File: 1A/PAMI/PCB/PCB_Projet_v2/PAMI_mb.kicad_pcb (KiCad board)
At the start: 4 copper layers, 65 x 56 mm, 106 parts, among them J101 Conn_02x20_Odd_Even, J102 Conn_01x03, J103 Conn_ST_STDC14, J104 Battery, J105 Charge, J106 Stop, J107 Conn_01x04, J108 173010542, J109 Conn_01x04, J110 Conn_01x04, J111 Conn_01x04, J112 Conn_01x04, SW101 SW_Push_SPDT, SW102 RotaryEncoder_Switch, SW103 SW_Push, SW401 SW_Push, SW501 SW_Push, SW601 SW_Push, U101 STM32G431KBTx, U102 LT1076CR-PBF, U103 AZ1117CH2-3.3TRG1, U201 TMC2225-SA-T, U301 TMC2225-SA-T

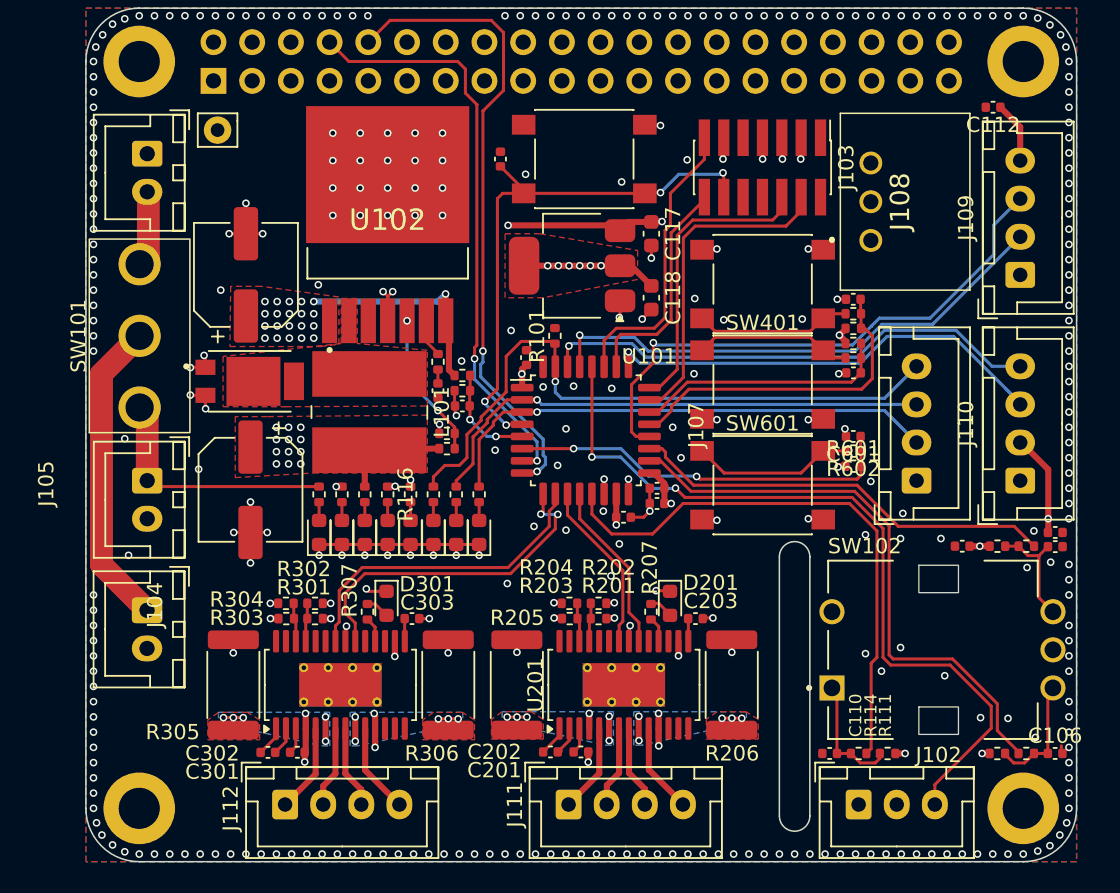
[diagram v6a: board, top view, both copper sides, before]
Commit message: update PCB Silkcreen
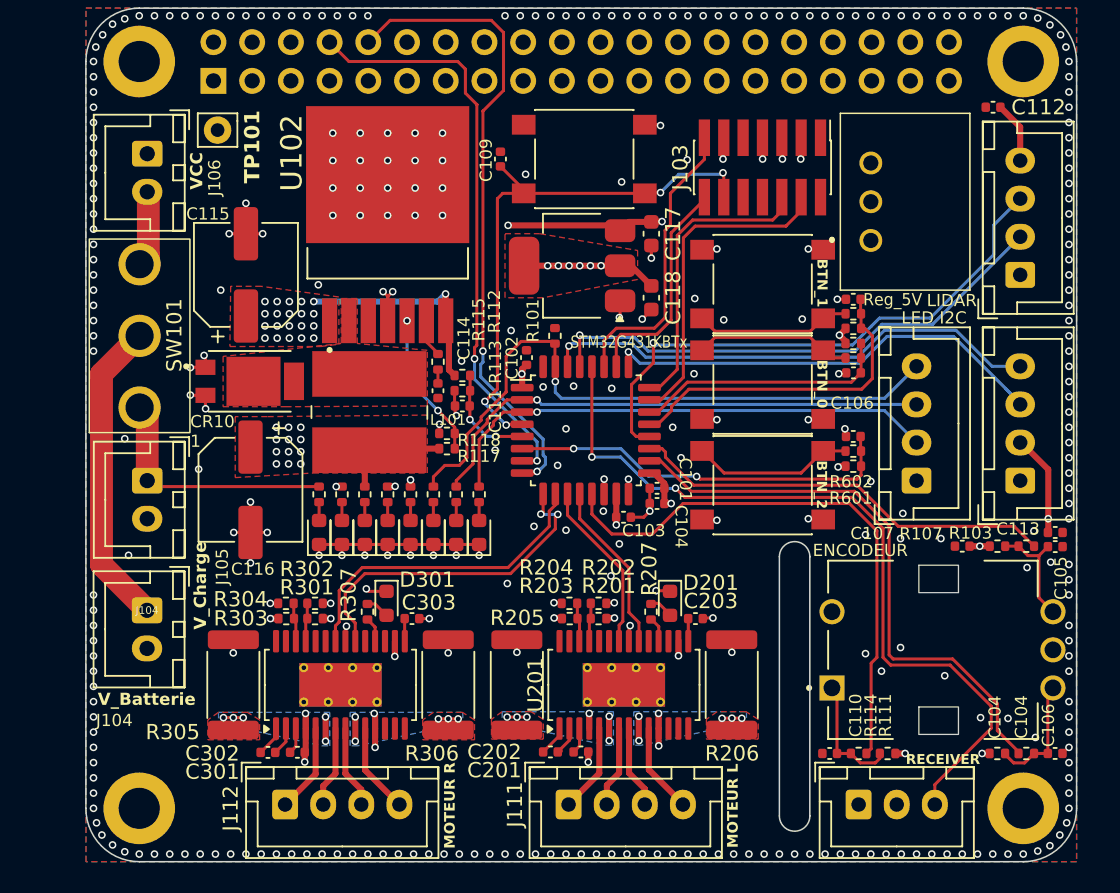
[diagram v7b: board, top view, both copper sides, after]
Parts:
- renumbered SW102 to ENCODEUR, J109 to LIDAR, J102 to RECEIVER, U101 to STM32G431KBTx
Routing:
- net GND: track 69.1 -> 68.6 mm
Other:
- board text added: "BTN_0"
- board text added: "BTN_1"
- board text added: "BTN_2"
- board text added: "C101"
- board text added: "C102"
- board text added: "C103"
- board text added: "C104"
- board text added: "C105"
- board text added: "C106"
- board text added: "C107"
- board text added: "C109"
- board text added: "C111"
- board text added: "C113"
- board text added: "C114"
- board text added: "C115"
- board text added: "C116"
- board text added: "CR10 1"
- board text added: "D101"
- board text added: "D102"
- board text added: "D103"
- board text added: "D104"
- board text added: "D105"
- board text added: "D106"
- board text added: "D107"
- board text added: "D108"
- board text added: "I2C"
- board text added: "J104"
- board text added: "J106"
- board text added: "LED"
- board text added: "MOTEUR L"
- board text added: "MOTEUR R"
- board text added: "R102"
- board text added: "R103"
- board text added: "R104"
- board text added: "R106"
- board text added: "R107"
- board text added: "R108"
- board text added: "R110"
- board text added: "R112"
- board text added: "R113"
- board text added: "R115"
- board text added: "R117"
- board text added: "R118"
- board text added: "R119"
- board text added: "R120"
- board text added: "R601"
- board text added: "R602"
- board text added: "Reg_5V"
- board text added: "SW601"
- board text added: "TP101"
- board text added: "VCC"
- board text added: "V_Batterie"
- board text added: "V_Charge"

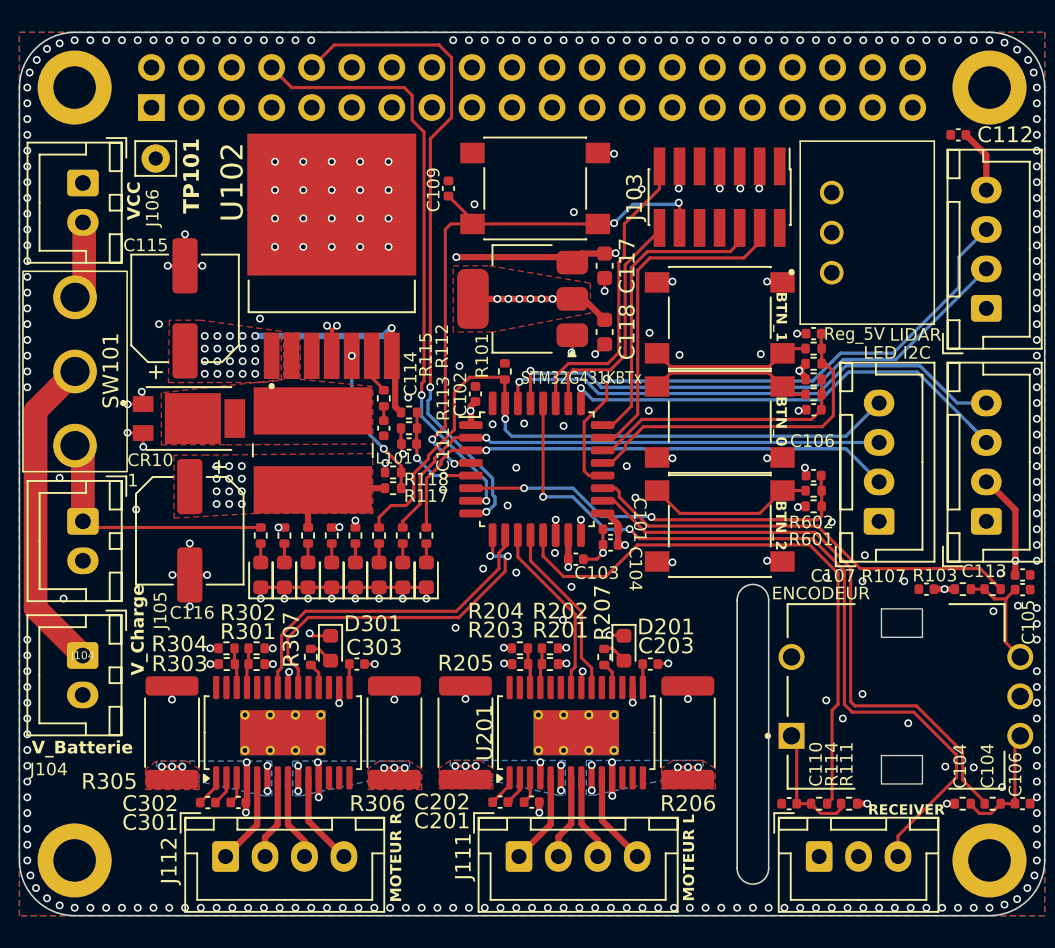
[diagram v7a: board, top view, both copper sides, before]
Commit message: update PCB Silkscreen
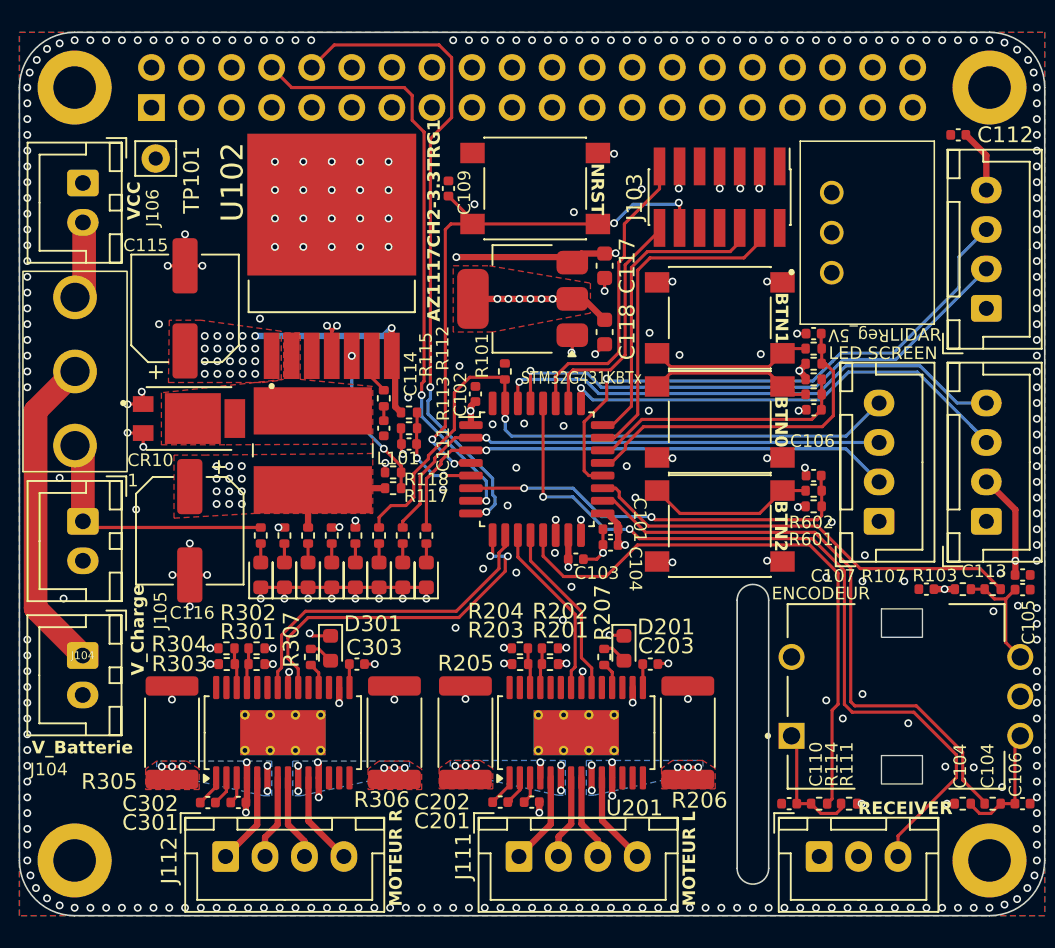
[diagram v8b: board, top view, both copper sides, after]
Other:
- board text added: "AZ1117CH2-3.3TRG1"
- board text added: "BTN0"
- board text added: "BTN1"
- board text added: "BTN2"
- board text added: "NRST"
- board text added: "SCREEN"
- board text added: "SW103"
- board text removed: "BTN_0"
- board text removed: "BTN_1"
- board text removed: "BTN_2"
- board text removed: "I2C"
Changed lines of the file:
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@@
 		(tags "resistor")
 		(property "Reference" "R116"
-			(at 0.040151 0.788143 270)
+			(at 0.040151 0.788143 -90)
 			(layer "B.SilkS")
 			(effects
@@
 		(tags "resistor")
 		(property "Reference" "R101"
-			(at 1 -1.442477 270)
+			(at 1 -1.442477 -90)
 			(layer "F.SilkS")
 			(effects
@@
 				(font
 					(size 1.4 1.4)
-					(thickness 0.15)
+					(thickness 0.2)
 				)
 			)
@@
 		(tags "resistor")
 		(property "Reference" "R206"
-			(at -4.5 0.025 0)
+			(at -4.28968 0.735407 0)
 			(layer "F.SilkS")
 			(effects
@@
 		(tags "connector JST XH vertical")
 		(property "Reference" "RECEIVER"
-			(at 5.53124 -2.963175 0)
+			(at 5.462581 -3.05864 0)
 			(layer "F.SilkS" knockout)
 			(effects
 				(font
-					(size 0.65 0.65)
+					(size 0.8 0.8)
 					(thickness 0.125)
 					(bold yes)
@@
 			(at 0.049282 2.27866 90)
 			(unlocked yes)
-			(layer "F.SilkS")
+			(layer "B.SilkS")
 			(effects
 				(font
@@
 					(thickness 0.1)
 				)
+				(justify mirror)
 			)
 		)
@@
 		(tags "resistor")
 		(property "Reference" "R306"
-			(at -4.5 -1.075 0)
+			(at -4.246477 -0.800908 0)
 			(layer "F.SilkS")
 			(effects
@@
 		(tags "HTSSOP SO")
 		(property "Reference" "U201"
-			(at 0 -5.8 -90)
+			(at -4.774704 3.690625 0)
 			(layer "F.SilkS")
 			(effects
@@
 		(tags "Choke Power Inductor WE-PD2 TypL Wuerth")
 		(property "Reference" "L101"
-			(at 0.514116 -5.160024 180)
+			(at 0.514116 -5.4 180)
 			(layer "F.SilkS")
 			(effects
 				(font
-					(size 0.7 0.7)
+					(size 0.8 0.8)
 					(thickness 0.15)
 				)
@@
 		(tags "resistor")
 		(property "Reference" "R602"
-			(at -1.15 -0.051702 270)
+			(at -1.15 -0.051702 -90)
 			(layer "F.SilkS")
 			(hide yes)
@@
 		)
 	)
+	(gr_text "SW103"
+		(at 161.819337 56.780738 0)
+		(layer "B.SilkS")
+		(effects
+			(font
+				(size 1 1)
+				(thickness 0.15)
+			)
+			(justify left bottom mirror)
+		)
+	)
 	(gr_text "D108"
 		(at 148.262923 82.605614 90)
@@
 		)
 	)
+	(gr_text "NRST"
+		(at 162.672215 54.788608 270)
+		(layer "F.SilkS")
+		(effects
+			(font
+				(size 0.8 0.8)
+				(thickness 0.2)
+				(bold yes)
+			)
+			(justify left bottom)
+		)
+	)
 	(gr_text "C104"
 		(at 186.610343 94.452818 90)
@@
 	)
 	(gr_text "R112"
-		(at 153.768899 67.822679 90)
+		(at 153.797157 67.954768 90)
 		(layer "F.SilkS")
 		(effects
@@
 		)
 	)
-	(gr_text "BTN_0"
-		(at 174.403692 69.560034 -90)
+	(gr_text "BTN0"
+		(at 174.313433 69.550519 270)
 		(layer "F.SilkS" knockout)
 		(effects
 			(font
-				(size 0.67 0.67)
+				(size 0.8 0.8)
 				(thickness 0.1675)
 				(bold yes)
@@
 	)
 	(gr_text "C109"
-		(at 153.224734 57.908091 90)
+		(at 155.1748 58.090408 90)
 		(layer "F.SilkS")
 		(effects
@@
 		)
 	)
-	(gr_text "BTN_2"
-		(at 174.380489 76.167315 -90)
+	(gr_text "BTN2"
+		(at 174.301377 76.171212 270)
 		(layer "F.SilkS" knockout)
 		(effects
 			(font
-				(size 0.67 0.67)
+				(size 0.8 0.8)
 				(thickness 0.1675)
 				(bold yes)
@@
 			(font
 				(size 1 1)
-				(thickness 0.2)
-				(bold yes)
+				(thickness 0.1)
 			)
 			(justify left bottom)
@@
 	)
 	(gr_text "LED"
-		(at 180 67.286825 0)
+		(at 177.795686 67.304999 0)
 		(layer "F.SilkS" knockout)
 		(effects
@@
 	)
 	(gr_text "MOTEUR R"
-		(at 150.78488 101.657029 90)
+		(at 150.831816 101.909537 90)
 		(layer "F.SilkS" knockout)
 		(effects
 			(font
-				(size 0.7 0.7)
+				(size 0.8 0.76)
 				(thickness 0.125)
 				(bold yes)
@@
 		)
 	)
+	(gr_text "AZ1117CH2-3.3TRG1"
+		(at 153.248634 64.845979 90)
+		(layer "F.SilkS")
+		(effects
+			(font
+				(size 0.8 0.8)
+				(thickness 0.2)
+				(bold yes)
+			)
+			(justify left bottom)
+		)
+	)
 	(gr_text "C106"
 		(at 175.348619 72.880489 0)
@@
 	)
 	(gr_text "MOTEUR L"
-		(at 169.352696 101.605055 90)
+		(at 169.430681 101.898404 90)
 		(layer "F.SilkS" knockout)
 		(effects
 			(font
-				(size 0.7 0.7)
+				(size 0.8 0.76)
 				(thickness 0.125)
 				(bold yes)
@@
 		)
 	)
-	(gr_text "I2C"
-		(at 182.5 67.286825 0)
+	(gr_text "SCREEN"
+		(at 180.27125 67.311931 0)
 		(layer "F.SilkS" knockout)
 		(effects
@@
 		)
 	)
-	(gr_text "BTN_1"
-		(at 174.413838 62.938578 -90)
+	(gr_text "BTN1"
+		(at 174.349311 62.981348 270)
 		(layer "F.SilkS" knockout)
 		(effects
 			(font
-				(size 0.67 0.67)
+				(size 0.8 0.8)
 				(thickness 0.1675)
 				(bold yes)
@@
 	)
 	(gr_text "Reg_5V"
-		(at 177.496389 66.091718 0)
+		(at 181.647312 65.241175 180)
 		(layer "F.SilkS")
 		(effects
@@
 	)
 	(segment
-		(start 179.61 95.4)
-		(end 180.25 95.4)
-		(width 0.4)
-		(layer "F.Cu")
-		(net 1)
-	)
-	(segment
 		(start 187.873414 75)
 		(end 188.286707 75.413293)
@@
 	)
 	(segment
+		(start 179.61 95.4)
+		(end 179.889091 95.4)
+		(width 0.4)
+		(layer "F.Cu")
+		(net 1)
+	)
+	(segment
 		(start 161.295 79.9)
 		(end 161.295 80.395)
@@
 	)
 	(segment
+		(start 185.3 95.4)
+		(end 185.79 95.4)
+		(width 0.4)
+		(layer "F.Cu")
+		(net 1)
+	)
+	(segment
 		(start 173.43 56.37)
 		(end 173.4 56.4)
@@
 	)
 	(segment
-		(start 185.3 95.4)
-		(end 185.79 95.4)
-		(width 0.4)
-		(layer "F.Cu")
-		(net 1)
-	)
-	(segment
 		(start 147.8 77.89)
 		(end 147.8 77.450002)
@@
 	)
 	(via
-		(at 180.25 95.4)
+		(at 179.889091 95.4)
 		(size 0.5)
 		(drill 0.3)
